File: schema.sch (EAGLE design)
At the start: 10 parts

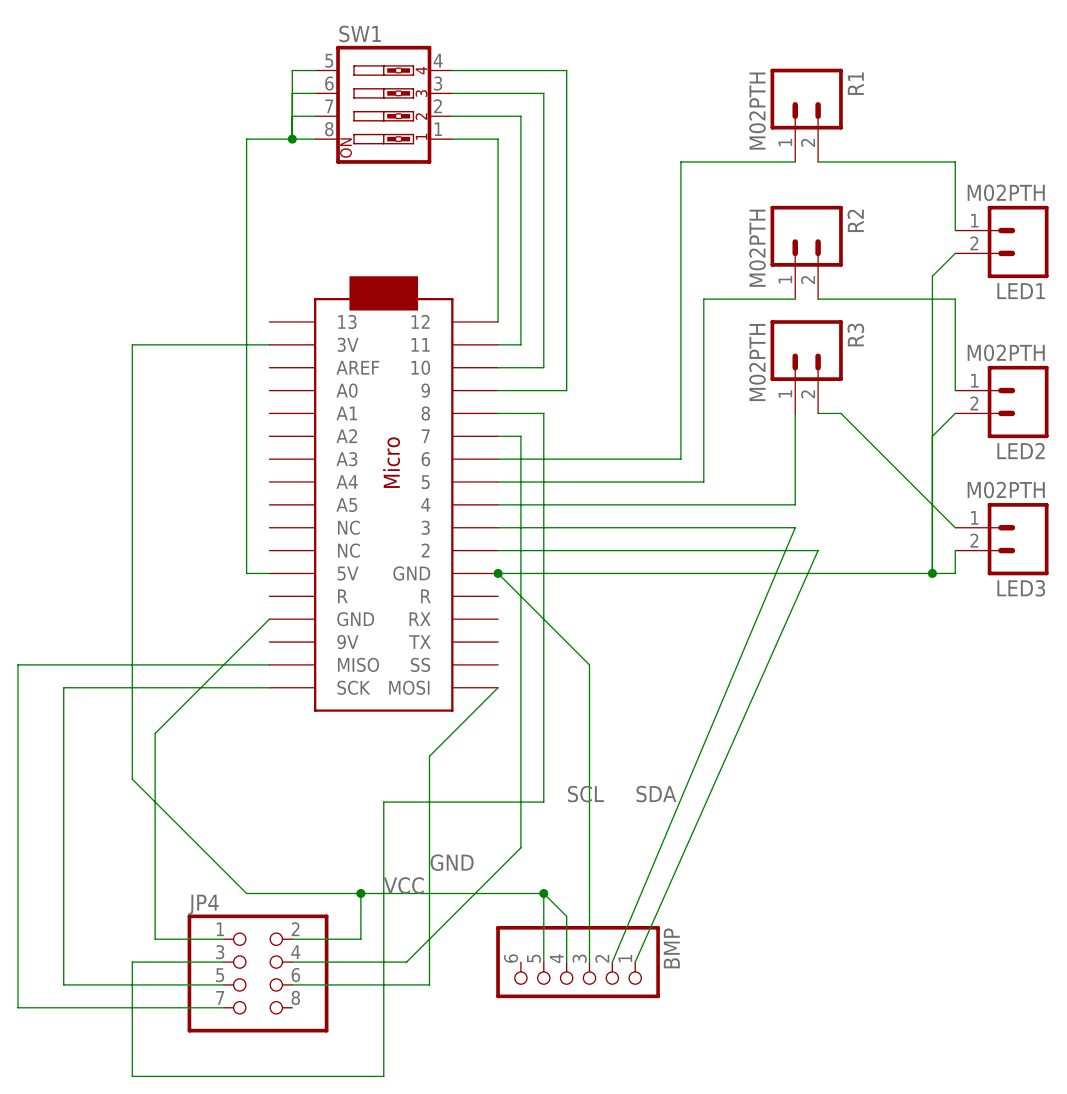
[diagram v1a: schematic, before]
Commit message: Add mounting holes
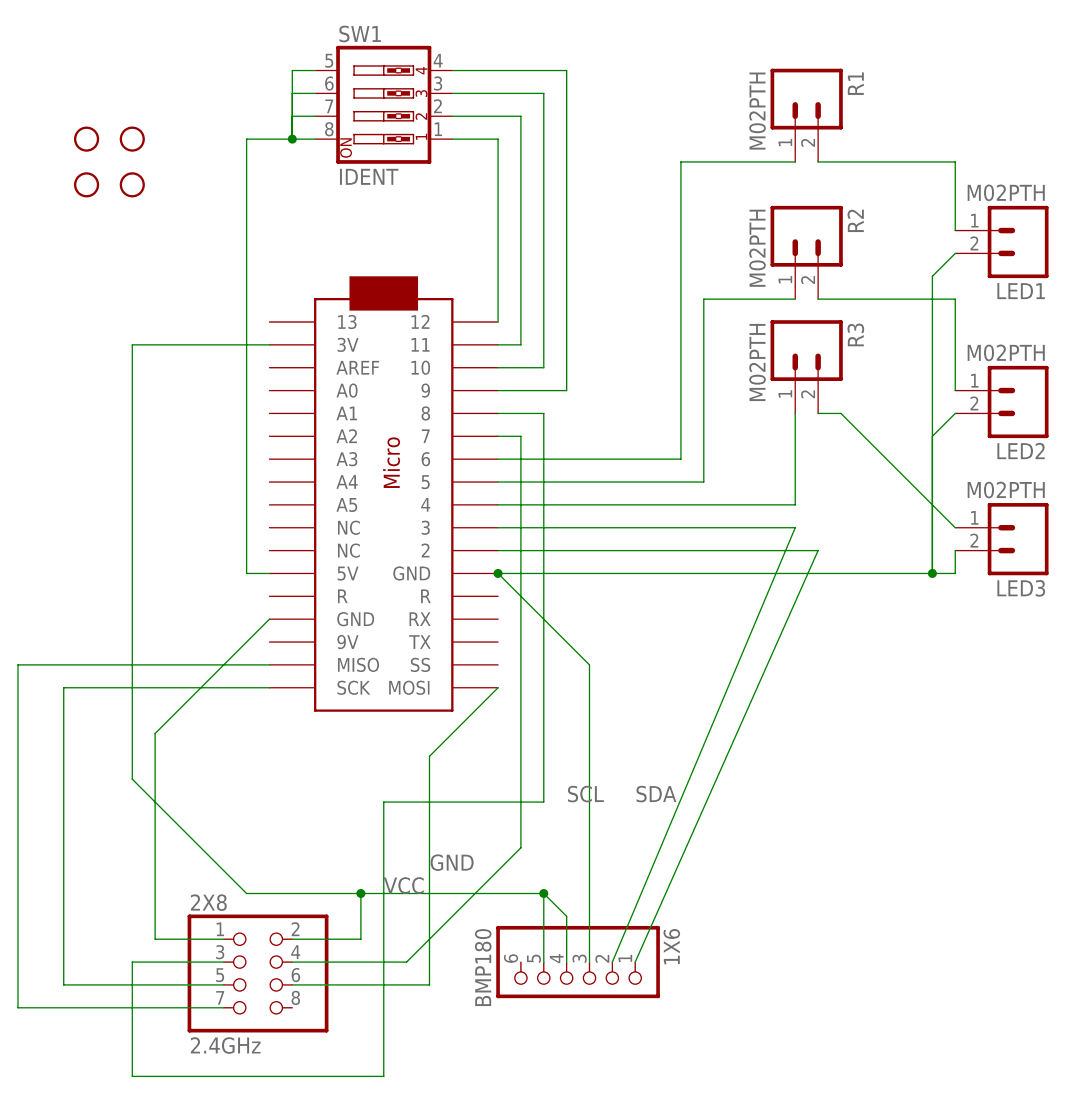
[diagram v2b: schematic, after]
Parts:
- added STANDOFF1, STANDOFF2, STANDOFF3, STANDOFF4: STAND-OFF, SparkFun-Electromechanical:STAND-OFF
- 1X6: value (none) -> BMP180
- 2X8: value (none) -> 2.4GHz
- SW1: value (none) -> IDENT
- renumbered BMP to 1X6, JP4 to 2X8
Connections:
- net N$11: now also R1.1
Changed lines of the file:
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@@
 <parts>
 <part name="U$1" library="adafruit" deviceset="ARDUINOMICRO" device=""/>
-<part name="JP4" library="adafruit" deviceset="PINHD-2X4" device=""/>
-<part name="BMP" library="adafruit" deviceset="PINHD-1X6" device=""/>
+<part name="2X8" library="adafruit" deviceset="PINHD-2X4" device="" value="2.4GHz"/>
+<part name="1X6" library="adafruit" deviceset="PINHD-1X6" device="" value="BMP180"/>
 <part name="LED1" library="SparkFun-Connectors" deviceset="M02" device="PTH"/>
 <part name="LED2" library="SparkFun-Connectors" deviceset="M02" device="PTH"/>
@@
 <part name="R2" library="SparkFun-Connectors" deviceset="M02" device="PTH"/>
 <part name="R3" library="SparkFun-Connectors" deviceset="M02" device="PTH"/>
-<part name="SW1" library="special" deviceset="SW_DIP-4" device=""/>
+<part name="SW1" library="special" deviceset="SW_DIP-4" device="" value="IDENT"/>
+<part name="STANDOFF1" library="SparkFun-Electromechanical" deviceset="STAND-OFF" device=""/>
+<part name="STANDOFF2" library="SparkFun-Electromechanical" deviceset="STAND-OFF" device=""/>
+<part name="STANDOFF3" library="SparkFun-Electromechanical" deviceset="STAND-OFF" device=""/>
+<part name="STANDOFF4" library="SparkFun-Electromechanical" deviceset="STAND-OFF" device=""/>
 </parts>
 <sheets>
@@
 <instances>
 <instance part="U$1" gate="G$1" x="38.1" y="55.88" rot="R270"/>
-<instance part="JP4" gate="A" x="22.86" y="2.54"/>
-<instance part="BMP" gate="A" x="58.42" y="2.54" smashed="yes" rot="R270">
+<instance part="2X8" gate="A" x="22.86" y="2.54"/>
+<instance part="1X6" gate="A" x="58.42" y="2.54" smashed="yes" rot="R270">
 <attribute name="NAME" x="69.215" y="8.89" size="1.778" layer="95" rot="R270"/>
 <attribute name="VALUE" x="48.26" y="8.89" size="1.778" layer="96" rot="R270"/>
@@
 <instance part="R3" gate="G$1" x="83.82" y="73.66" rot="R270"/>
 <instance part="SW1" gate="A" x="38.1" y="101.6"/>
+<instance part="STANDOFF1" gate="G$1" x="5.08" y="96.52"/>
+<instance part="STANDOFF2" gate="G$1" x="10.16" y="96.52"/>
+<instance part="STANDOFF3" gate="G$1" x="10.16" y="91.44"/>
+<instance part="STANDOFF4" gate="G$1" x="5.08" y="91.44"/>
 </instances>
 <busses>
@@
 <wire x1="10.16" y1="73.66" x2="10.16" y2="25.4" width="0.1524" layer="91"/>
 <wire x1="10.16" y1="25.4" x2="22.86" y2="12.7" width="0.1524" layer="91"/>
-<pinref part="BMP" gate="A" pin="5"/>
+<pinref part="1X6" gate="A" pin="5"/>
 <wire x1="22.86" y1="12.7" x2="35.56" y2="12.7" width="0.1524" layer="91"/>
 <wire x1="35.56" y1="12.7" x2="55.88" y2="12.7" width="0.1524" layer="91"/>
 <wire x1="55.88" y1="12.7" x2="55.88" y2="5.08" width="0.1524" layer="91"/>
-<pinref part="BMP" gate="A" pin="4"/>
+<pinref part="1X6" gate="A" pin="4"/>
 <wire x1="55.88" y1="12.7" x2="58.42" y2="10.16" width="0.1524" layer="91"/>
 <wire x1="58.42" y1="10.16" x2="58.42" y2="5.08" width="0.1524" layer="91"/>
@@
 <pinref part="U$1" gate="G$1" pin="3V"/>
 <wire x1="10.16" y1="73.66" x2="25.4" y2="73.66" width="0.1524" layer="91"/>
-<pinref part="JP4" gate="A" pin="2"/>
+<pinref part="2X8" gate="A" pin="2"/>
 <wire x1="35.56" y1="12.7" x2="35.56" y2="7.62" width="0.1524" layer="91"/>
 <wire x1="35.56" y1="7.62" x2="27.94" y2="7.62" width="0.1524" layer="91"/>
@@
 <net name="SCL" class="0">
 <segment>
-<pinref part="BMP" gate="A" pin="2"/>
+<pinref part="1X6" gate="A" pin="2"/>
 <wire x1="63.5" y1="5.08" x2="83.82" y2="53.34" width="0.1524" layer="91"/>
 <label x="58.42" y="22.86" size="1.778" layer="95"/>
@@
 <net name="SDA" class="0">
 <segment>
-<pinref part="BMP" gate="A" pin="1"/>
+<pinref part="1X6" gate="A" pin="1"/>
 <wire x1="86.36" y1="50.8" x2="66.04" y2="5.08" width="0.1524" layer="91"/>
 <label x="66.04" y="22.86" size="1.778" layer="95"/>
@@
 <wire x1="25.4" y1="43.18" x2="12.7" y2="30.48" width="0.1524" layer="91"/>
 <wire x1="12.7" y1="30.48" x2="12.7" y2="7.62" width="0.1524" layer="91"/>
-<pinref part="JP4" gate="A" pin="1"/>
+<pinref part="2X8" gate="A" pin="1"/>
 <wire x1="12.7" y1="7.62" x2="20.32" y2="7.62" width="0.1524" layer="91"/>
 </segment>
 <segment>
-<pinref part="BMP" gate="A" pin="3"/>
+<pinref part="1X6" gate="A" pin="3"/>
 <label x="43.18" y="15.24" size="1.778" layer="95"/>
 <pinref part="U$1" gate="G$1" pin="GND@1"/>
@@
 <wire x1="38.1" y1="-7.62" x2="10.16" y2="-7.62" width="0.1524" layer="91"/>
 <wire x1="10.16" y1="-7.62" x2="10.16" y2="5.08" width="0.1524" layer="91"/>
-<pinref part="JP4" gate="A" pin="3"/>
+<pinref part="2X8" gate="A" pin="3"/>
 <wire x1="10.16" y1="5.08" x2="20.32" y2="5.08" width="0.1524" layer="91"/>
 </segment>
@@
 <wire x1="53.34" y1="63.5" x2="53.34" y2="17.78" width="0.1524" layer="91"/>
 <wire x1="53.34" y1="17.78" x2="40.64" y2="5.08" width="0.1524" layer="91"/>
-<pinref part="JP4" gate="A" pin="4"/>
+<pinref part="2X8" gate="A" pin="4"/>
 <wire x1="40.64" y1="5.08" x2="27.94" y2="5.08" width="0.1524" layer="91"/>
 </segment>
@@
 <wire x1="25.4" y1="35.56" x2="2.54" y2="35.56" width="0.1524" layer="91"/>
 <wire x1="2.54" y1="35.56" x2="2.54" y2="2.54" width="0.1524" layer="91"/>
-<pinref part="JP4" gate="A" pin="5"/>
+<pinref part="2X8" gate="A" pin="5"/>
 <wire x1="2.54" y1="2.54" x2="20.32" y2="2.54" width="0.1524" layer="91"/>
 </segment>
@@
 <wire x1="50.8" y1="35.56" x2="43.18" y2="27.94" width="0.1524" layer="91"/>
 <wire x1="43.18" y1="27.94" x2="43.18" y2="2.54" width="0.1524" layer="91"/>
-<pinref part="JP4" gate="A" pin="6"/>
+<pinref part="2X8" gate="A" pin="6"/>
 <wire x1="43.18" y1="2.54" x2="27.94" y2="2.54" width="0.1524" layer="91"/>
 </segment>
@@
 <pinref part="U$1" gate="G$1" pin="MISO"/>
 <wire x1="25.4" y1="38.1" x2="-2.54" y2="38.1" width="0.1524" layer="91"/>
-<pinref part="JP4" gate="A" pin="7"/>
+<pinref part="2X8" gate="A" pin="7"/>
 <wire x1="-2.54" y1="38.1" x2="-2.54" y2="0" width="0.1524" layer="91"/>
 <wire x1="-2.54" y1="0" x2="20.32" y2="0" width="0.1524" layer="91"/>
@@
 <pinref part="R2" gate="G$1" pin="1"/>
 <wire x1="73.66" y1="78.74" x2="83.82" y2="78.74" width="0.1524" layer="91"/>
-</segment>
-</net>
-<net name="N$11" class="0">
-<segment>
-<pinref part="U$1" gate="G$1" pin="6"/>
-<wire x1="50.8" y1="60.96" x2="71.12" y2="60.96" width="0.1524" layer="91"/>
-<wire x1="71.12" y1="60.96" x2="71.12" y2="93.98" width="0.1524" layer="91"/>
-<wire x1="71.12" y1="93.98" x2="83.82" y2="93.98" width="0.1524" layer="91"/>
 </segment>
 </net>
@@
 </segment>
 </net>
-<net name="N$14" class="0">
-<segment>
-<wire x1="45.72" y1="99.06" x2="53.34" y2="99.06" width="0.1524" layer="91"/>
-<wire x1="53.34" y1="99.06" x2="53.34" y2="73.66" width="0.1524" layer="91"/>
-<pinref part="U$1" gate="G$1" pin="11"/>
-<wire x1="53.34" y1="73.66" x2="50.8" y2="73.66" width="0.1524" layer="91"/>
-<pinref part="SW1" gate="A" pin="2"/>
-</segment>
-</net>
 <net name="N$15" class="0">
 <segment>
@@
 </segment>
 </net>
+<net name="N$11" class="0">
+<segment>
+<pinref part="U$1" gate="G$1" pin="6"/>
+<wire x1="50.8" y1="60.96" x2="71.12" y2="60.96" width="0.1524" layer="91"/>
+<wire x1="71.12" y1="60.96" x2="71.12" y2="93.98" width="0.1524" layer="91"/>
+<pinref part="R1" gate="G$1" pin="1"/>
+<wire x1="71.12" y1="93.98" x2="83.82" y2="93.98" width="0.1524" layer="91"/>
+</segment>
+</net>
+<net name="N$14" class="0">
+<segment>
+<pinref part="SW1" gate="A" pin="2"/>
+<wire x1="45.72" y1="99.06" x2="53.34" y2="99.06" width="0.1524" layer="91"/>
+<wire x1="53.34" y1="99.06" x2="53.34" y2="73.66" width="0.1524" layer="91"/>
+<pinref part="U$1" gate="G$1" pin="11"/>
+<wire x1="53.34" y1="73.66" x2="50.8" y2="73.66" width="0.1524" layer="91"/>
+</segment>
+</net>
